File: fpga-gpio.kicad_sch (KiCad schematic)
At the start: 32 parts, among them Q5 DMG1012T-7, Q7 DMG1012T-7, Q8 DMG1012T-7, U1 MPFS250T-FCVG484, U14 NTS0102_XSON, U18 74LVC1T45GM, U19 NTS0102_XSON, U20 NTS0102_XSON, U21 NTS0102_XSON, U24 NTS0102_XSON, U25 NTS0102_XSON, U27 NTS0102_XSON, U29 NTS0102_XSON

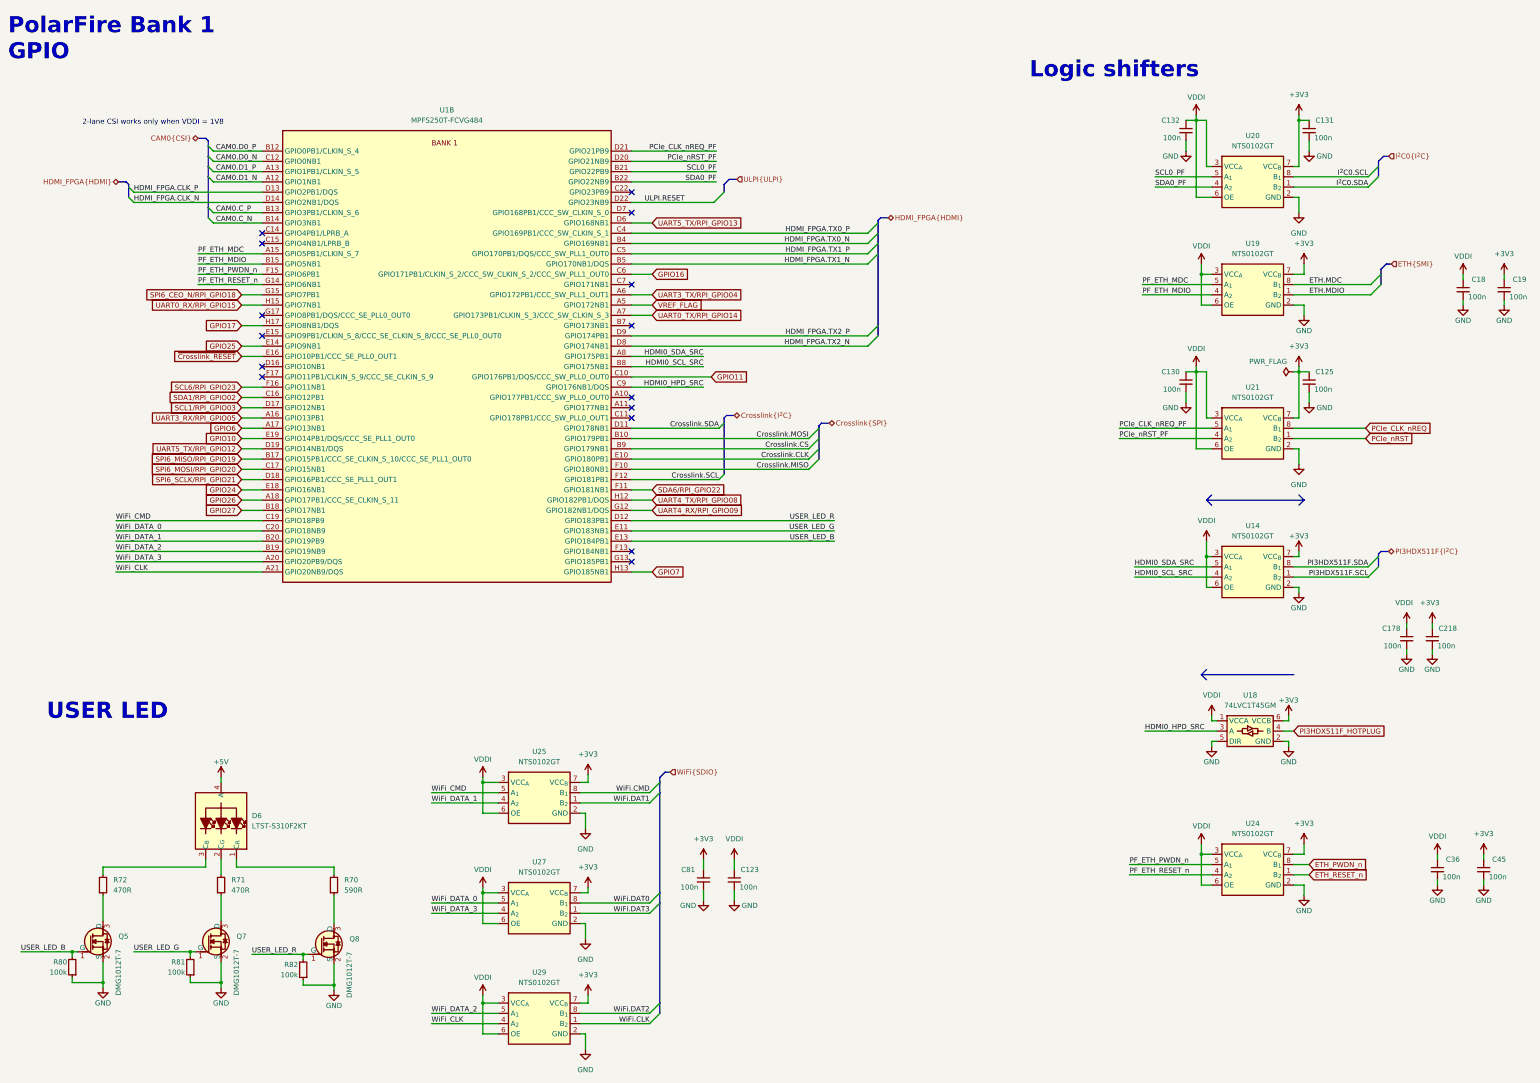
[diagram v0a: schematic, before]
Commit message: [#59910] Align buses, updated symbols and clean ERC
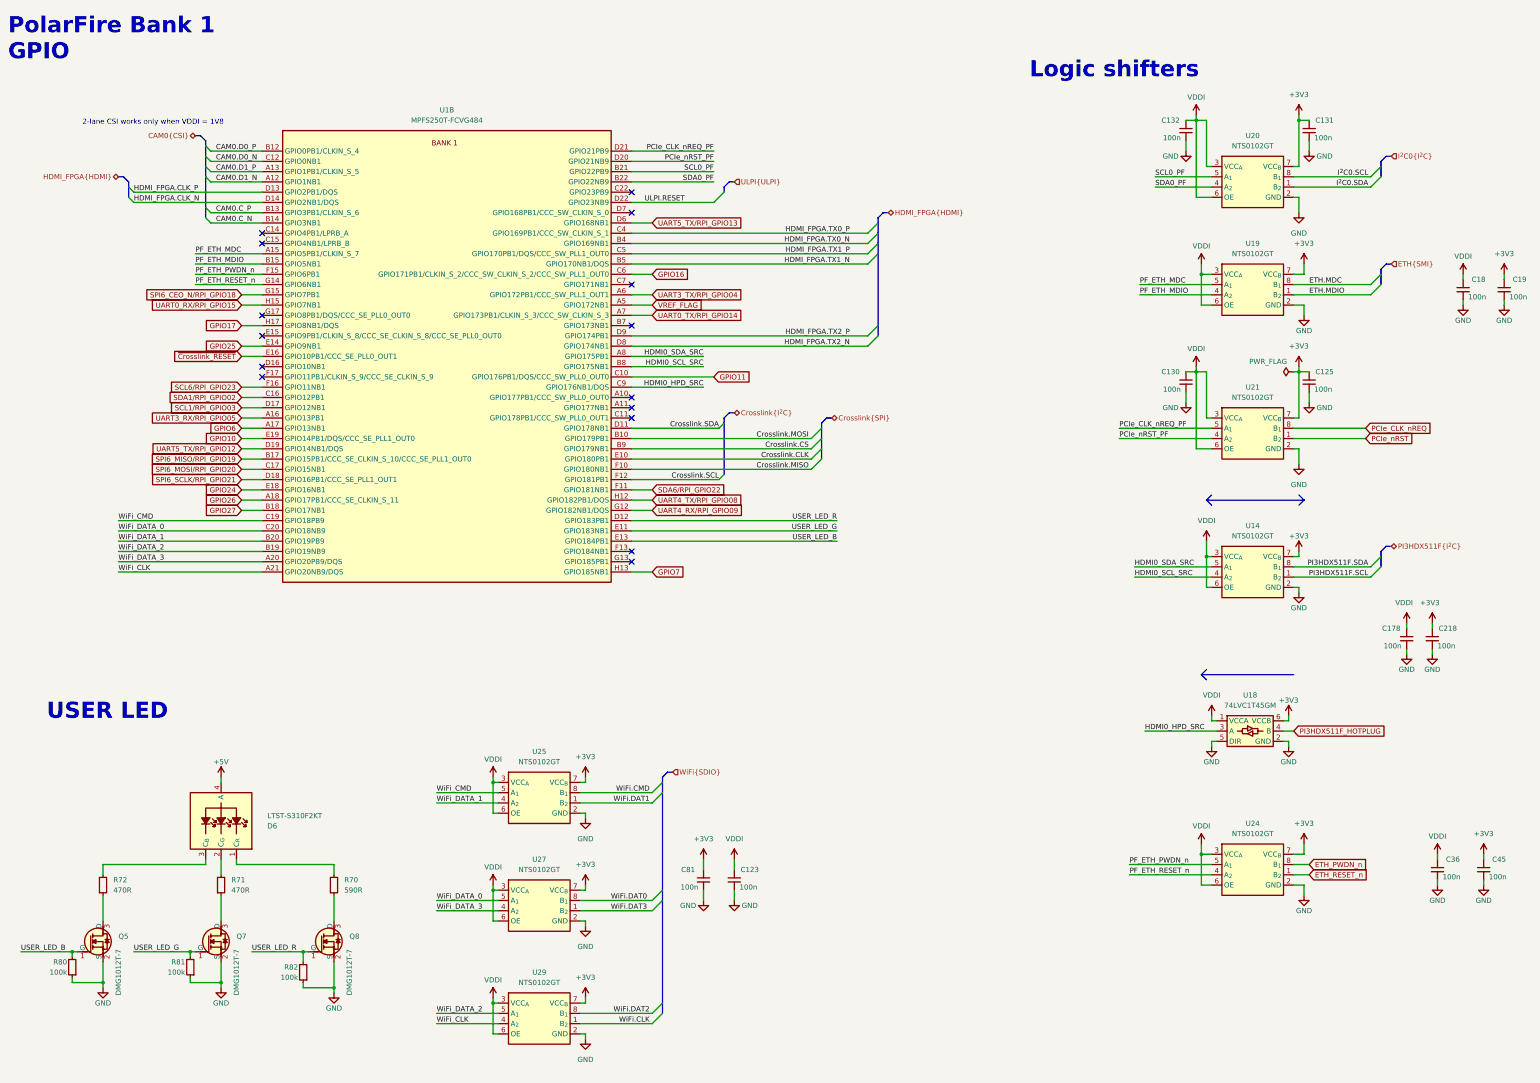
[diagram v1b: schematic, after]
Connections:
- net VDDI renamed VDD
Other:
- moved on the sheet: Q8, R82, U27

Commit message: [#73079] Migrate project to KiCad 8. Clean DRCs
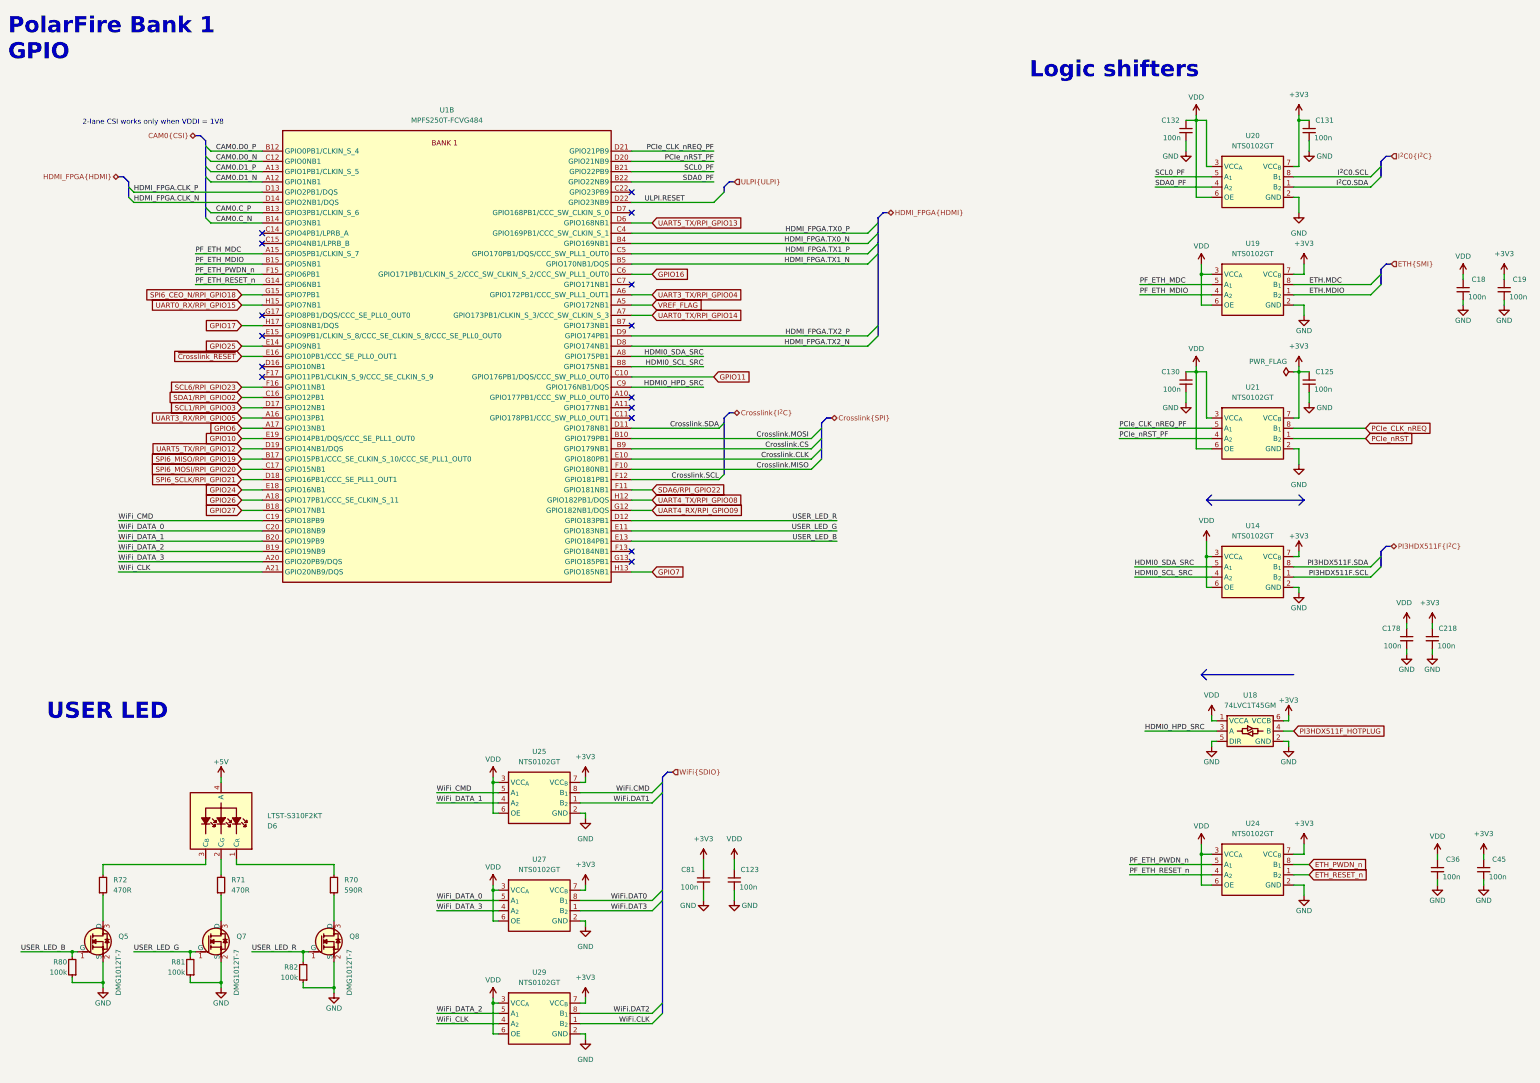
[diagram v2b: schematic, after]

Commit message: [#73079] Update symbols, clean ERC
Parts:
- D6: footprint antmicro-footprints:LED_1204_3210Metric_RGB -> antmicro-footprints:LED_1204_3210Metric_RGB_Horizontal
